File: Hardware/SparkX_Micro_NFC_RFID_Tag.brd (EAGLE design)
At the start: 7.6 x 31.8 mm, 31 parts, among them J1 QWIIC_RIGHT_ANGLE, U1 ST25DV64KC

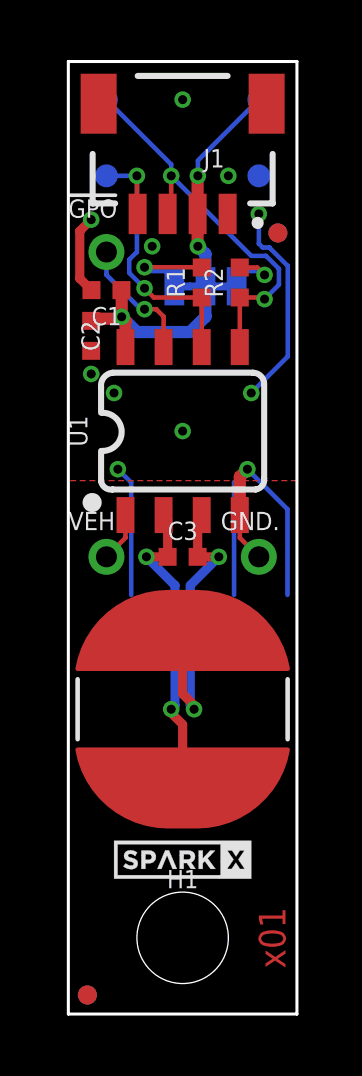
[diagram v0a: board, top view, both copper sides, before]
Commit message: Remove GND from under antenna
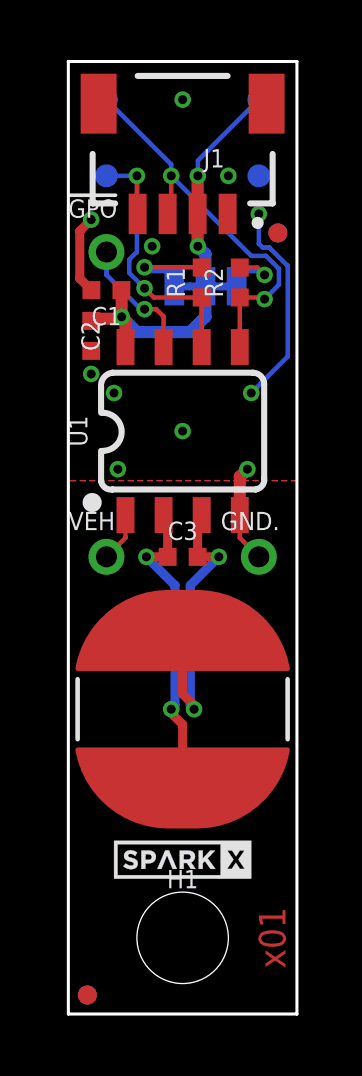
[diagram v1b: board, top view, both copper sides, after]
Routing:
- net GND: track 26.5 -> 13.0 mm
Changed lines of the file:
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@@
 <drawing>
 <settings>
-<setting alwaysvectorfont="yes"/>
+<setting alwaysvectorfont="no"/>
 <setting verticaltext="up"/>
 </settings>
@@
 <vertex x="0" y="31.75"/>
 <vertex x="7.62" y="31.75"/>
-<vertex x="7.62" y="0"/>
-<vertex x="0" y="0"/>
+<vertex x="7.62" y="17.78"/>
+<vertex x="0" y="17.78"/>
 </polygon>
 <contactref element="C2" pad="2"/>
@@
 <wire x1="6.70034375" y1="25.5524" x2="7.3152" y2="24.93754375" width="0.1524" layer="16"/>
 <wire x1="7.3152" y1="24.93754375" x2="7.3152" y2="21.9202" width="0.1524" layer="16"/>
-<wire x1="5.969" y1="18.161" x2="7.3025" y2="16.8275" width="0.1524" layer="16"/>
-<wire x1="7.3025" y1="16.8275" x2="7.3025" y2="13.97" width="0.1524" layer="16"/>
-<wire x1="1.651" y1="18.161" x2="2.0955" y2="17.7165" width="0.1524" layer="16"/>
-<wire x1="2.0955" y1="17.7165" x2="2.0955" y2="13.97" width="0.1524" layer="16"/>
-<wire x1="5.969" y1="18.161" x2="5.5245" y2="17.7165" width="0.1524" layer="16"/>
-<wire x1="5.5245" y1="17.7165" x2="5.5245" y2="13.97" width="0.1524" layer="16"/>
 </signal>
 <signal name="EDAP">
